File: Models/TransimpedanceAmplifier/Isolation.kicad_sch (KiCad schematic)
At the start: 10 parts, among them U11 ISO7641FM, U12 ISO7641FM

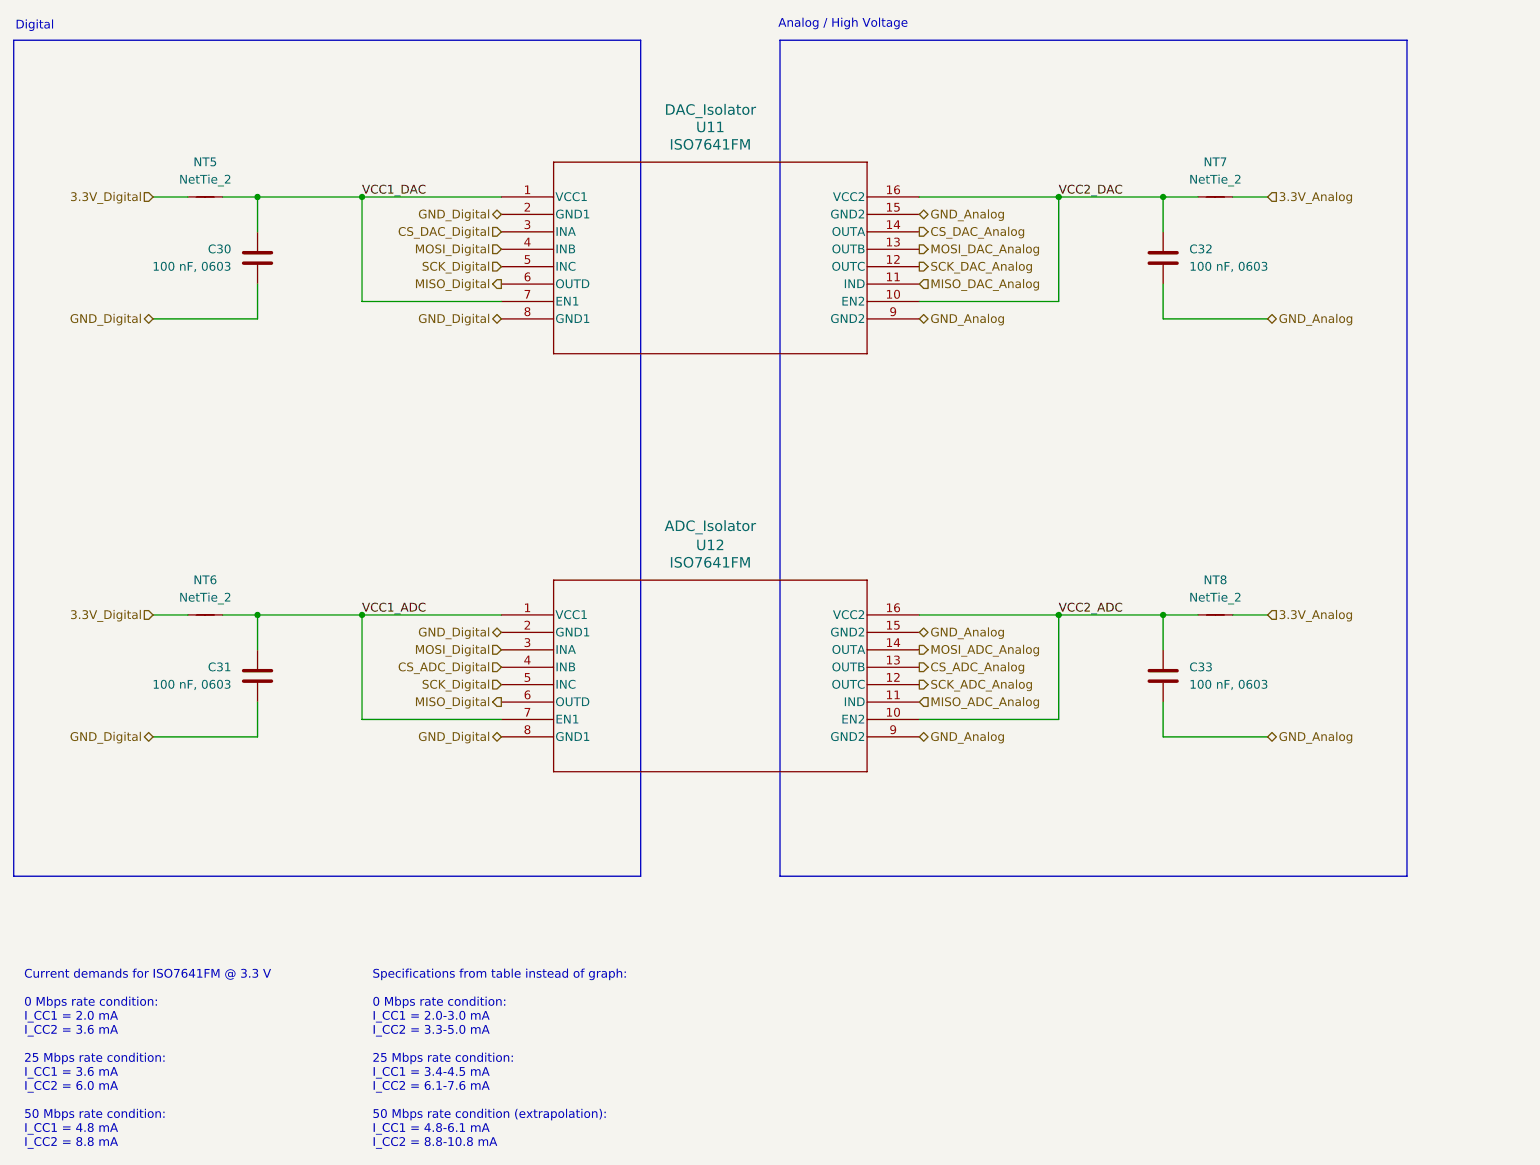
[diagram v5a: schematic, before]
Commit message: Finished the isolator decoupling networks
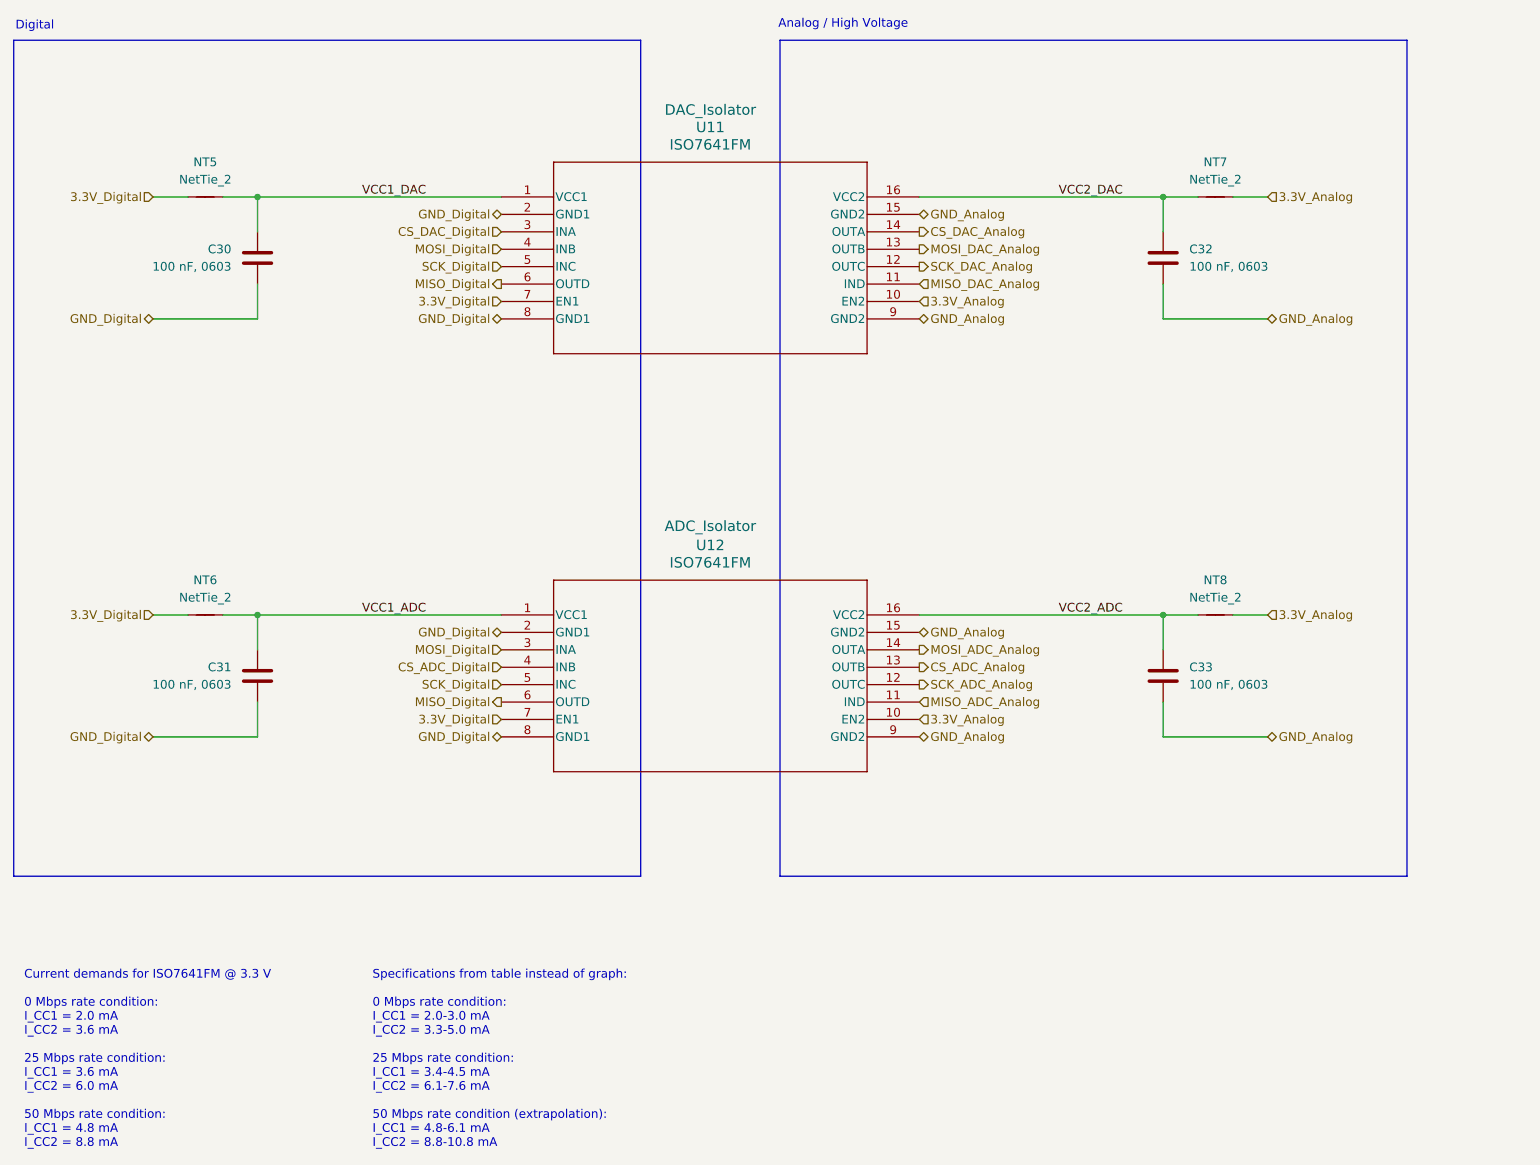
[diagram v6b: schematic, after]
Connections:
- net 3.3V_Analog: now also U11.10 (EN2), U12.10 (EN2)
- net 3.3V_Digital: now also U11.7 (EN1), U12.7 (EN1)
- net VCC1_ADC: no longer U12.7 (EN1)
- net VCC1_DAC: no longer U11.7 (EN1)
- net VCC2_ADC: no longer U12.10 (EN2)
- net VCC2_DAC: no longer U11.10 (EN2)
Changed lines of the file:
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@@
-	)
-	(junction
-		(at 203.2 45.72)
-		(diameter 0)
-		(color 0 0 0 0)
-	)
-	(junction
-		(at 203.2 106.68)
-		(diameter 0)
-		(color 0 0 0 0)
-	)
-	(junction
-		(at 101.6 45.72)
-		(diameter 0)
-		(color 0 0 0 0)
 	)
 	(junction
@@
 	)
 	(junction
-		(at 101.6 106.68)
-		(diameter 0)
-		(color 0 0 0 0)
-	)
-	(junction
 		(at 86.36 106.68)
 		(diameter 0)
@@
 	(wire
 		(pts
-			(xy 182.88 121.92) (xy 203.2 121.92)
-		)
-		(stroke
-			(width 0)
-			(type default)
-		)
-	)
-	(wire
-		(pts
 			(xy 228.6 45.72) (xy 233.68 45.72)
 		)
@@
 	(wire
 		(pts
-			(xy 101.6 121.92) (xy 121.92 121.92)
-		)
-		(stroke
-			(width 0)
-			(type default)
-		)
-	)
-	(wire
-		(pts
-			(xy 101.6 106.68) (xy 101.6 121.92)
-		)
-		(stroke
-			(width 0)
-			(type default)
-		)
-	)
-	(wire
-		(pts
 			(xy 81.28 106.68) (xy 86.36 106.68)
 		)
@@
 	(wire
 		(pts
-			(xy 182.88 60.96) (xy 203.2 60.96)
-		)
-		(stroke
-			(width 0)
-			(type default)
-		)
-	)
-	(wire
-		(pts
-			(xy 182.88 45.72) (xy 203.2 45.72)
-		)
-		(stroke
-			(width 0)
-			(type default)
-		)
-	)
-	(wire
-		(pts
 			(xy 228.6 106.68) (xy 233.68 106.68)
 		)
@@
 	(wire
 		(pts
-			(xy 86.36 106.68) (xy 101.6 106.68)
-		)
-		(stroke
-			(width 0)
-			(type default)
-		)
-	)
-	(wire
-		(pts
-			(xy 203.2 106.68) (xy 203.2 121.92)
+			(xy 86.36 106.68) (xy 121.92 106.68)
 		)
 		(stroke
@@
 	(wire
 		(pts
-			(xy 101.6 60.96) (xy 121.92 60.96)
-		)
-		(stroke
-			(width 0)
-			(type default)
-		)
-	)
-	(wire
-		(pts
-			(xy 203.2 45.72) (xy 218.44 45.72)
-		)
-		(stroke
-			(width 0)
-			(type default)
-		)
-	)
-	(wire
-		(pts
-			(xy 203.2 45.72) (xy 203.2 60.96)
+			(xy 182.88 45.72) (xy 218.44 45.72)
 		)
 		(stroke
@@
 	(wire
 		(pts
-			(xy 101.6 45.72) (xy 101.6 60.96)
-		)
-		(stroke
-			(width 0)
-			(type default)
-		)
-	)
-	(wire
-		(pts
 			(xy 81.28 45.72) (xy 86.36 45.72)
 		)
@@
 	(wire
 		(pts
-			(xy 86.36 45.72) (xy 101.6 45.72)
+			(xy 86.36 45.72) (xy 121.92 45.72)
 		)
 		(stroke
@@
 	(wire
 		(pts
-			(xy 101.6 45.72) (xy 121.92 45.72)
-		)
-		(stroke
-			(width 0)
-			(type default)
-		)
-	)
-	(wire
-		(pts
-			(xy 101.6 106.68) (xy 121.92 106.68)
-		)
-		(stroke
-			(width 0)
-			(type default)
-		)
-	)
-	(wire
-		(pts
 			(xy 218.44 45.72) (xy 218.44 50.8)
 		)
@@
 	(wire
 		(pts
-			(xy 203.2 106.68) (xy 218.44 106.68)
-		)
-		(stroke
-			(width 0)
-			(type default)
-		)
-	)
-	(wire
-		(pts
-			(xy 182.88 106.68) (xy 203.2 106.68)
+			(xy 182.88 106.68) (xy 218.44 106.68)
 		)
 		(stroke
@@
 		)
 	)
+	(hierarchical_label "3.3V_Analog"
+		(shape input)
+		(at 182.88 121.92 0)
+		(effects
+			(font
+				(size 1.27 1.27)
+			)
+			(justify left)
+		)
+	)
+	(hierarchical_label "3.3V_Analog"
+		(shape input)
+		(at 182.88 60.96 0)
+		(effects
+			(font
+				(size 1.27 1.27)
+			)
+			(justify left)
+		)
+	)
 	(hierarchical_label "MOSI_Digital"
 		(shape input)
@@
 	(hierarchical_label "3.3V_Digital"
 		(shape input)
+		(at 121.92 60.96 180)
+		(effects
+			(font
+				(size 1.27 1.27)
+			)
+			(justify right)
+		)
+	)
+	(hierarchical_label "3.3V_Digital"
+		(shape input)
 		(at 71.12 45.72 180)
 		(effects
@@
 		)
 	)
+	(hierarchical_label "3.3V_Digital"
+		(shape input)
+		(at 121.92 121.92 180)
+		(effects
+			(font
+				(size 1.27 1.27)
+			)
+			(justify right)
+		)
+	)
